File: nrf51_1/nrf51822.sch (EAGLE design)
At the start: 22 parts, among them T1 MMUN2238

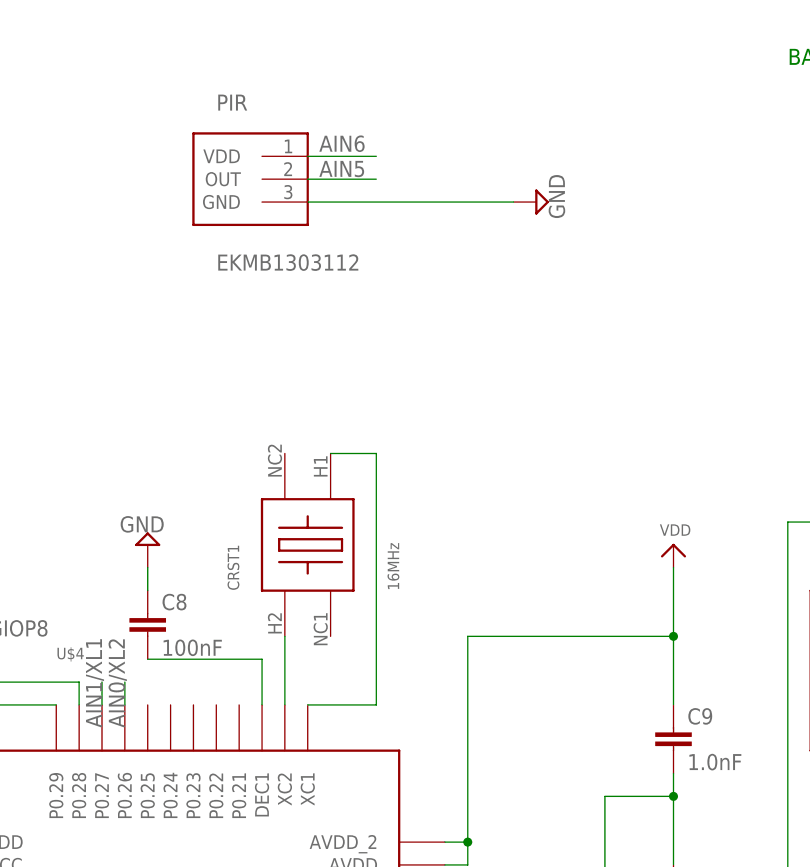
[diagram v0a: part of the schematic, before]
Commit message: Sensor board should be 100% done... Waiting for boards from slow china :0)
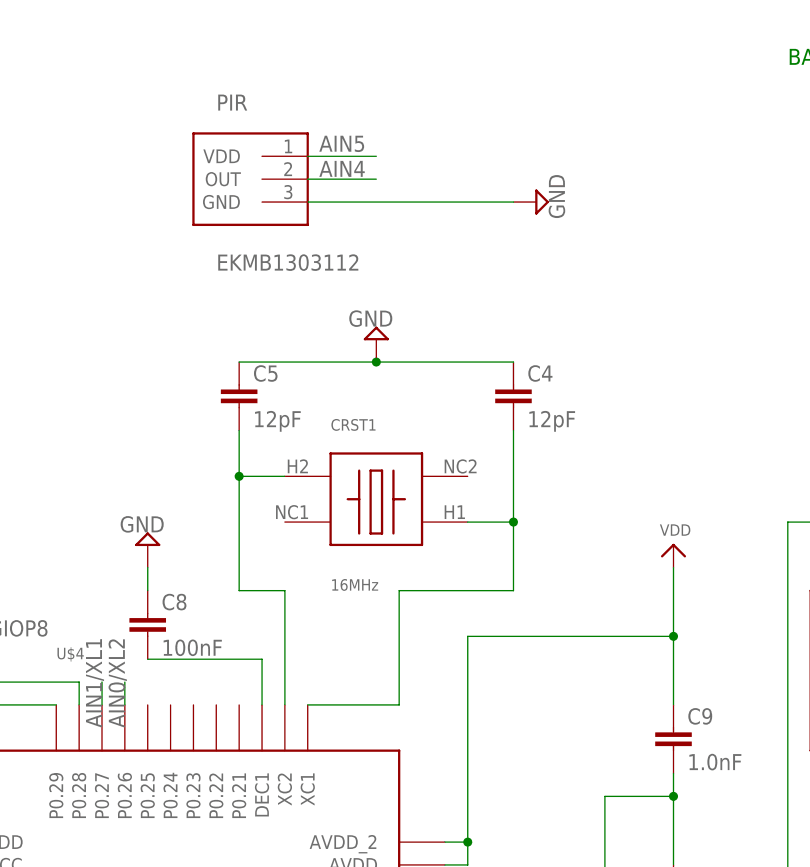
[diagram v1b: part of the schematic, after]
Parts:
- added C4, C5: 12pF, rcl:C-EUC0805
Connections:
- net AIN4: now also PIR.OUT
- net AIN5: now also PIR.VDD; no longer PIR.OUT
- net AIN6: no longer PIR.VDD
- net GND: now also C4.1, C5.1
- net N$1: now also C5.2, CRST1.H2, U$4.XC2; no longer CRST1.H1, U$4.XC1
- net N$2: now also C4.2, CRST1.H1, U$4.XC1; no longer CRST1.H2, U$4.XC2
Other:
- moved on the sheet: CRST1
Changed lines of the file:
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@@
 <part name="SW1" library="microbuilder" deviceset="SWITCH_PUSHBUTTON" device="SOFTTOUCHSMD_SJ"/>
 <part name="SUPPLY16" library="supply2" deviceset="GND" device=""/>
+<part name="SUPPLY17" library="supply2" deviceset="GND" device=""/>
+<part name="C4" library="rcl" deviceset="C-EU" device="C0805" value="12pF"/>
+<part name="C5" library="rcl" deviceset="C-EU" device="C0805" value="12pF"/>
 </parts>
 <sheets>
@@
 <instance part="SUPPLY11" gate="GND" x="137.16" y="63.5"/>
 <instance part="SUPPLY12" gate="GND" x="132.08" y="99.06" rot="R180"/>
-<instance part="CRST1" gate="G$1" x="68.58" y="93.98" rot="R90"/>
+<instance part="CRST1" gate="G$1" x="76.2" y="99.06"/>
 <instance part="SUPPLY4" gate="GND" x="137.16" y="144.78" rot="R270"/>
 <instance part="AA" gate="G$1" x="134.62" y="124.46" rot="R90"/>
@@
 <instance part="SW1" gate="G$1" x="17.78" y="-2.54"/>
 <instance part="SUPPLY16" gate="GND" x="5.08" y="-2.54" rot="R270"/>
+<instance part="SUPPLY17" gate="GND" x="76.2" y="116.84" rot="R180"/>
+<instance part="C4" gate="G$1" x="91.44" y="111.76"/>
+<instance part="C5" gate="G$1" x="60.96" y="111.76"/>
 </instances>
 <busses>
@@
 <wire x1="12.7" y1="-2.54" x2="7.62" y2="-2.54" width="0.1524" layer="91"/>
 </segment>
-</net>
-<net name="N$2" class="0">
-<segment>
-<pinref part="U$4" gate="G$1" pin="XC2"/>
-<wire x1="66.04" y1="83.82" x2="66.04" y2="76.2" width="0.1524" layer="91"/>
-<pinref part="CRST1" gate="G$1" pin="H2"/>
+<segment>
+<pinref part="C5" gate="G$1" pin="1"/>
+<pinref part="SUPPLY17" gate="GND" pin="GND"/>
+<wire x1="60.96" y1="114.3" x2="76.2" y2="114.3" width="0.1524" layer="91"/>
+<pinref part="C4" gate="G$1" pin="1"/>
+<wire x1="91.44" y1="114.3" x2="76.2" y2="114.3" width="0.1524" layer="91"/>
+<junction x="76.2" y="114.3"/>
 </segment>
 </net>
@@
 <pinref part="BALUN" gate="G$1" pin="BAL2"/>
 <wire x1="127" y1="68.58" x2="127" y2="48.26" width="0.1524" layer="91"/>
-</segment>
-</net>
-<net name="N$1" class="0">
-<segment>
-<pinref part="U$4" gate="G$1" pin="XC1"/>
-<wire x1="68.58" y1="76.2" x2="76.2" y2="76.2" width="0.1524" layer="91"/>
-<wire x1="76.2" y1="76.2" x2="76.2" y2="104.14" width="0.1524" layer="91"/>
-<pinref part="CRST1" gate="G$1" pin="H1"/>
-<wire x1="76.2" y1="104.14" x2="71.12" y2="104.14" width="0.1524" layer="91"/>
 </segment>
 </net>
@@
 <label x="20.32" y="45.72" size="1.778" layer="95"/>
 </segment>
+<segment>
+<pinref part="PIR" gate="G$1" pin="OUT"/>
+<wire x1="68.58" y1="134.62" x2="76.2" y2="134.62" width="0.1524" layer="91"/>
+<label x="69.85" y="134.874" size="1.778" layer="95"/>
+</segment>
 </net>
 <net name="AIN5" class="0">
@@
 </segment>
 <segment>
-<pinref part="PIR" gate="G$1" pin="OUT"/>
-<wire x1="68.58" y1="134.62" x2="76.2" y2="134.62" width="0.1524" layer="91"/>
-<label x="69.85" y="134.874" size="1.778" layer="95"/>
+<pinref part="PIR" gate="G$1" pin="VDD"/>
+<wire x1="68.58" y1="137.16" x2="76.2" y2="137.16" width="0.1524" layer="91"/>
+<label x="69.85" y="137.668" size="1.778" layer="95"/>
 </segment>
 </net>
@@
 <wire x1="25.4" y1="40.64" x2="22.86" y2="40.64" width="0.1524" layer="91"/>
 <label x="22.86" y="40.64" size="1.778" layer="95"/>
-</segment>
-<segment>
-<pinref part="PIR" gate="G$1" pin="VDD"/>
-<wire x1="68.58" y1="137.16" x2="76.2" y2="137.16" width="0.1524" layer="91"/>
-<label x="69.85" y="137.668" size="1.778" layer="95"/>
 </segment>
 </net>
@@
 </segment>
 </net>
+<net name="N$1" class="0">
+<segment>
+<pinref part="CRST1" gate="G$1" pin="H2"/>
+<pinref part="C5" gate="G$1" pin="2"/>
+<wire x1="66.04" y1="101.6" x2="60.96" y2="101.6" width="0.1524" layer="91"/>
+<wire x1="60.96" y1="101.6" x2="60.96" y2="106.68" width="0.1524" layer="91"/>
+<wire x1="60.96" y1="101.6" x2="60.96" y2="88.9" width="0.1524" layer="91"/>
+<junction x="60.96" y="101.6"/>
+<pinref part="U$4" gate="G$1" pin="XC2"/>
+<wire x1="60.96" y1="88.9" x2="66.04" y2="88.9" width="0.1524" layer="91"/>
+<wire x1="66.04" y1="88.9" x2="66.04" y2="76.2" width="0.1524" layer="91"/>
+</segment>
+</net>
+<net name="N$2" class="0">
+<segment>
+<pinref part="C4" gate="G$1" pin="2"/>
+<pinref part="U$4" gate="G$1" pin="XC1"/>
+<wire x1="68.58" y1="76.2" x2="78.74" y2="76.2" width="0.1524" layer="91"/>
+<wire x1="78.74" y1="76.2" x2="78.74" y2="88.9" width="0.1524" layer="91"/>
+<wire x1="78.74" y1="88.9" x2="91.44" y2="88.9" width="0.1524" layer="91"/>
+<wire x1="91.44" y1="88.9" x2="91.44" y2="96.52" width="0.1524" layer="91"/>
+<pinref part="CRST1" gate="G$1" pin="H1"/>
+<wire x1="91.44" y1="96.52" x2="91.44" y2="106.68" width="0.1524" layer="91"/>
+<wire x1="86.36" y1="96.52" x2="91.44" y2="96.52" width="0.1524" layer="91"/>
+<junction x="91.44" y="96.52"/>
+</segment>
+</net>

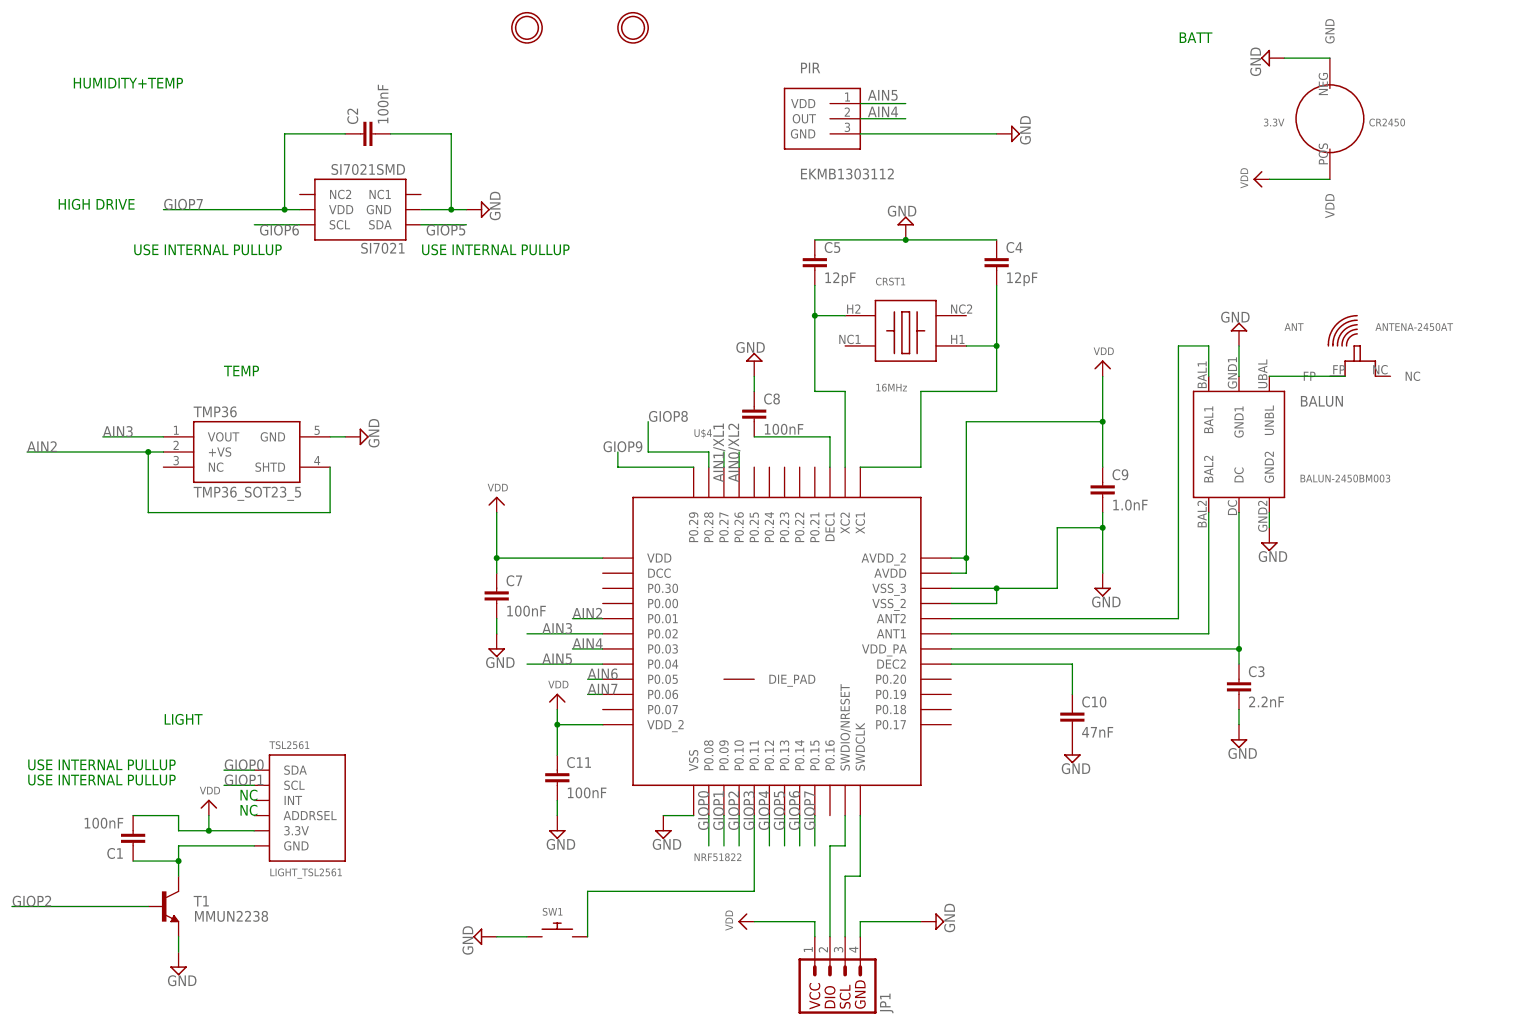
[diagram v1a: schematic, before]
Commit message: CLEANED AND ADDED COMMENTS / TAGS ACTUATION MADE 45% SMALLER
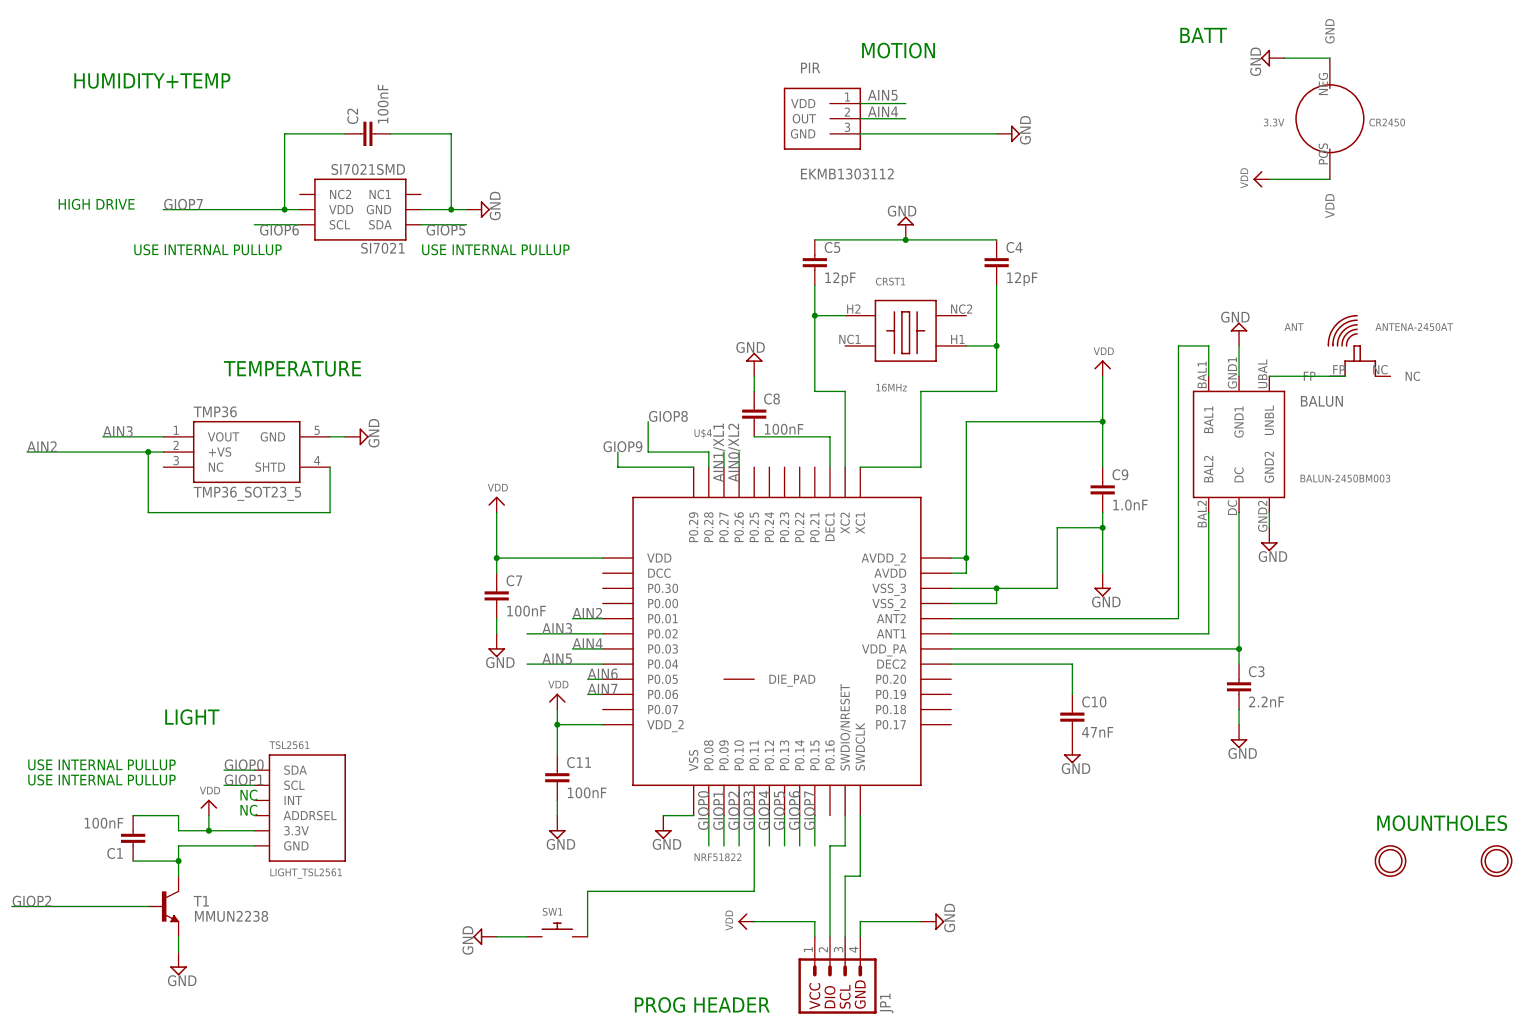
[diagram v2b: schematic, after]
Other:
- note added: "MOTION"
- note added: "MOUNTHOLES"
- note added: "PROG HEADER"
- note added: "TEMPERATURE"
- note removed: "TEMP"
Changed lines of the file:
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@@
 <setting verticaltext="up"/>
 </settings>
-<grid distance="0.1" unitdist="inch" unit="inch" style="lines" multiple="1" display="no" altdistance="0.01" altunitdist="inch" altunit="inch"/>
+<grid distance="0.1" unitdist="inch" unit="mm" style="lines" multiple="1" display="no" altdistance="0.01" altunitdist="inch" altunit="inch"/>
 <layers>
 <layer number="1" name="Top" color="4" fill="1" visible="no" active="no"/>
@@
 <text x="-71.12" y="25.4" size="1.778" layer="91">USE INTERNAL PULLUP</text>
 <text x="-71.12" y="22.86" size="1.778" layer="91">USE INTERNAL PULLUP</text>
-<text x="-48.26" y="33.02" size="1.778" layer="91">LIGHT</text>
-<text x="-38.1" y="91.44" size="1.778" layer="91">TEMP</text>
-<text x="121.92" y="147.32" size="1.778" layer="91">BATT</text>
+<text x="-48.26" y="33.02" size="2.54" layer="91">LIGHT</text>
+<text x="-38.1" y="91.44" size="2.54" layer="91">TEMPERATURE</text>
+<text x="121.92" y="147.32" size="2.54" layer="91">BATT</text>
 <text x="-66.04" y="119.38" size="1.778" layer="91">HIGH DRIVE</text>
 <text x="-53.34" y="111.76" size="1.778" layer="91">USE INTERNAL PULLUP</text>
 <text x="-5.08" y="111.76" size="1.778" layer="91">USE INTERNAL PULLUP</text>
-<text x="-63.5" y="139.7" size="1.778" layer="91">HUMIDITY+TEMP</text>
+<text x="-63.5" y="139.7" size="2.54" layer="91">HUMIDITY+TEMP</text>
+<text x="154.94" y="15.24" size="2.54" layer="91">MOUNTHOLES</text>
+<text x="68.58" y="144.78" size="2.54" layer="91">MOTION</text>
+<text x="30.48" y="-15.24" size="2.54" layer="91">PROG HEADER</text>
 </plain>
 <instances>
@@
 <instance part="PIR" gate="G$1" x="60.96" y="134.62"/>
 <instance part="SUPPLY15" gate="GND" x="93.98" y="132.08" rot="R90"/>
-<instance part="U$6" gate="G$1" x="12.7" y="149.86"/>
-<instance part="U$7" gate="G$1" x="30.48" y="149.86"/>
+<instance part="U$6" gate="G$1" x="157.48" y="10.16"/>
+<instance part="U$7" gate="G$1" x="175.26" y="10.16"/>
 <instance part="SW1" gate="G$1" x="17.78" y="-2.54"/>
 <instance part="SUPPLY16" gate="GND" x="5.08" y="-2.54" rot="R270"/>
